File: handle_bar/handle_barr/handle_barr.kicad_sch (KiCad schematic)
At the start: 18 parts, among them J1 SPKR, J2 MAX98357A 3V3, J3 HRN_SW, J4 BAT, J5 PS2, J6 USB, U1 XIAO_ESP32C3, U2 MCP73831-2-OT

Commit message: add joystick support on case
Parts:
- added GPS1: NEO6M, solderwirepad_1_02_SMD:SolderWirePad_1x04_SMD_1x3mm, symbol Connector_Generic:Conn_01x04
- renumbered R2 to R1, R1 to R2
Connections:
- net +3.3V: now also GPS1.1 (Pin_1)
- net GND: now also GPS1.4 (Pin_4)
- net SW_JS: now also U1.3 (D2); no longer U1.8 (RX_D7)
- net RX: now reaches U1.7 (TX_D6)
- net RX: now also GPS1.2 (Pin_2)
- new net TX: GPS1.3 (Pin_3), U1.8 (RX_D7)
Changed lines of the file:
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@@
     (stroke (width 0) (type default) (color 0 0 0 0))
   )
+  (global_label "RX" (shape input) (at 52.07 87.63 180) (fields_autoplaced)
+    (effects (font (size 1 1)) (justify right))
+    (property "Intersheet References" "${INTERSHEET_REFS}" (id 0) (at 48.2176 87.5675 0)
+      (effects (font (size 1 1)) (justify right) hide)
+    )
+  )
   (global_label "VDD" (shape input) (at 255.27 29.21 180) (fields_autoplaced)
     (effects (font (size 1 1)) (justify right))
@@
     (effects (font (size 1 1)) (justify left))
     (property "Intersheet References" "${INTERSHEET_REFS}" (id 0) (at 212.751 105.4725 0)
-      (effects (font (size 1 1)) (justify left) hide)
-    )
-  )
-  (global_label "SW_JS" (shape input) (at 78.74 48.26 0) (fields_autoplaced)
-    (effects (font (size 1 1)) (justify left))
-    (property "Intersheet References" "${INTERSHEET_REFS}" (id 0) (at 85.2114 48.3225 0)
       (effects (font (size 1 1)) (justify left) hide)
     )
@@
     )
   )
+  (global_label "SW_JS" (shape input) (at 43.18 50.8 180) (fields_autoplaced)
+    (effects (font (size 1 1)) (justify right))
+    (property "Intersheet References" "${INTERSHEET_REFS}" (id 0) (at 36.7086 50.7375 0)
+      (effects (font (size 1 1)) (justify right) hide)
+    )
+  )
+  (global_label "3V3" (shape input) (at 52.07 85.09 180) (fields_autoplaced)
+    (effects (font (size 1 1)) (justify right))
+    (property "Intersheet References" "${INTERSHEET_REFS}" (id 0) (at 47.4081 85.0275 0)
+      (effects (font (size 1 1)) (justify right) hide)
+    )
+  )
   (global_label "LED_DIN" (shape input) (at 104.14 43.18 180) (fields_autoplaced)
     (effects (font (size 1 1)) (justify right))
@@
     )
   )
+  (global_label "TX" (shape input) (at 52.07 90.17 180) (fields_autoplaced)
+    (effects (font (size 1 1)) (justify right))
+    (property "Intersheet References" "${INTERSHEET_REFS}" (id 0) (at 48.4557 90.1075 0)
+      (effects (font (size 1 1)) (justify right) hide)
+    )
+  )
   (global_label "DIN" (shape input) (at 43.18 53.34 180) (fields_autoplaced)
     (effects (font (size 1 1)) (justify right))
@@
     )
   )
+  (global_label "RX" (shape input) (at 78.74 45.72 0) (fields_autoplaced)
+    (effects (font (size 1 1)) (justify left))
+    (property "Intersheet References" "${INTERSHEET_REFS}" (id 0) (at 82.5924 45.7825 0)
+      (effects (font (size 1 1)) (justify left) hide)
+    )
+  )
+  (global_label "TX" (shape input) (at 78.74 48.26 0) (fields_autoplaced)
+    (effects (font (size 1 1)) (justify left))
+    (property "Intersheet References" "${INTERSHEET_REFS}" (id 0) (at 82.3543 48.3225 0)
+      (effects (font (size 1 1)) (justify left) hide)
+    )
+  )
   (global_label "GND" (shape input) (at 161.29 50.8 270) (fields_autoplaced)
     (effects (font (size 1 1)) (justify right))
@@
     (effects (font (size 1 1)) (justify right))
     (property "Intersheet References" "${INTERSHEET_REFS}" (id 0) (at 201.269 93.9175 0)
+      (effects (font (size 1 1)) (justify right) hide)
+    )
+  )
+  (global_label "GND" (shape input) (at 52.07 92.71 180) (fields_autoplaced)
+    (effects (font (size 1 1)) (justify right))
+    (property "Intersheet References" "${INTERSHEET_REFS}" (id 0) (at 47.1224 92.6475 0)
       (effects (font (size 1 1)) (justify right) hide)
     )
@@
     (pin "2")
   )
+  (symbol (lib_id "Connector_Generic:Conn_01x04") (at 57.15 87.63 0) (unit 1)
+    (in_bom yes) (on_board yes) (fields_autoplaced)
+    (property "Reference" "GPS1" (id 0) (at 59.69 87.6299 0)
+      (effects (font (size 1.27 1.27)) (justify left))
+    )
+    (property "Value" "NEO6M" (id 1) (at 59.69 90.1699 0)
+      (effects (font (size 1.27 1.27)) (justify left))
+    )
+    (property "Footprint" "solderwirepad_1_02_SMD:SolderWirePad_1x04_SMD_1x3mm" (id 2) (at 57.15 87.63 0)
+      (effects (font (size 1.27 1.27)) hide)
+    )
+    (property "Datasheet" "~" (id 3) (at 57.15 87.63 0)
+      (effects (font (size 1.27 1.27)) hide)
+    )
+    (pin "1")
+    (pin "2")
+    (pin "3")
+    (pin "4")
+  )
   (symbol (lib_id "power:GND") (at 238.76 82.55 0) (unit 1)
     (in_bom yes) (on_board yes) (fields_autoplaced)
@@
   (symbol (lib_id "Device:R") (at 149.86 99.06 0) (unit 1)
     (in_bom yes) (on_board yes)
-    (property "Reference" "R1" (id 0) (at 152.4 97.7899 0)
+    (property "Reference" "R2" (id 0) (at 152.4 97.7899 0)
       (effects (font (size 1.27 1.27)) (justify left))
     )
@@
   (symbol (lib_id "Device:R") (at 124.46 60.96 0) (unit 1)
     (in_bom yes) (on_board yes)
-    (property "Reference" "R2" (id 0) (at 127 59.6899 0)
+    (property "Reference" "R1" (id 0) (at 127 59.6899 0)
       (effects (font (size 1.27 1.27)) (justify left))
     )
@@
       (reference "D3") (unit 1) (value "WS2812B") (footprint "LED_SMD:LED_WS2812B_PLCC4_5.0x5.0mm_P3.2mm")
     )
+    (path "/14bdadf0-0709-4db7-9ed8-923b0e90bab6"
+      (reference "GPS1") (unit 1) (value "NEO6M") (footprint "solderwirepad_1_02_SMD:SolderWirePad_1x04_SMD_1x3mm")
+    )
     (path "/e1e1705c-e817-43c7-a6f2-583284baedae"
       (reference "J1") (unit 1) (value "SPKR") (footprint "")
@@
       (reference "PWR1") (unit 1) (value "SW_SPST") (footprint "solderwirepad_1_02_SMD:SolderWirePad_1x02_SMD_5x5mm")
     )
+    (path "/6d0b0be1-d31b-48c6-a8f6-1f65e558fbc9"
+      (reference "R1") (unit 1) (value "220ko") (footprint "Resistor_THT:R_Axial_DIN0207_L6.3mm_D2.5mm_P7.62mm_Horizontal")
+    )
     (path "/38f240f4-b45a-498e-b92b-89acdf6f6e3d"
-      (reference "R1") (unit 1) (value "2kΩ") (footprint "Resistor_THT:R_Axial_DIN0207_L6.3mm_D2.5mm_P7.62mm_Horizontal")
-    )
-    (path "/6d0b0be1-d31b-48c6-a8f6-1f65e558fbc9"
-      (reference "R2") (unit 1) (value "220ko") (footprint "Resistor_THT:R_Axial_DIN0207_L6.3mm_D2.5mm_P7.62mm_Horizontal")
+      (reference "R2") (unit 1) (value "2kΩ") (footprint "Resistor_THT:R_Axial_DIN0207_L6.3mm_D2.5mm_P7.62mm_Horizontal")
     )
     (path "/9e8719a0-1e3e-4a7f-a6ab-4c947d699615"

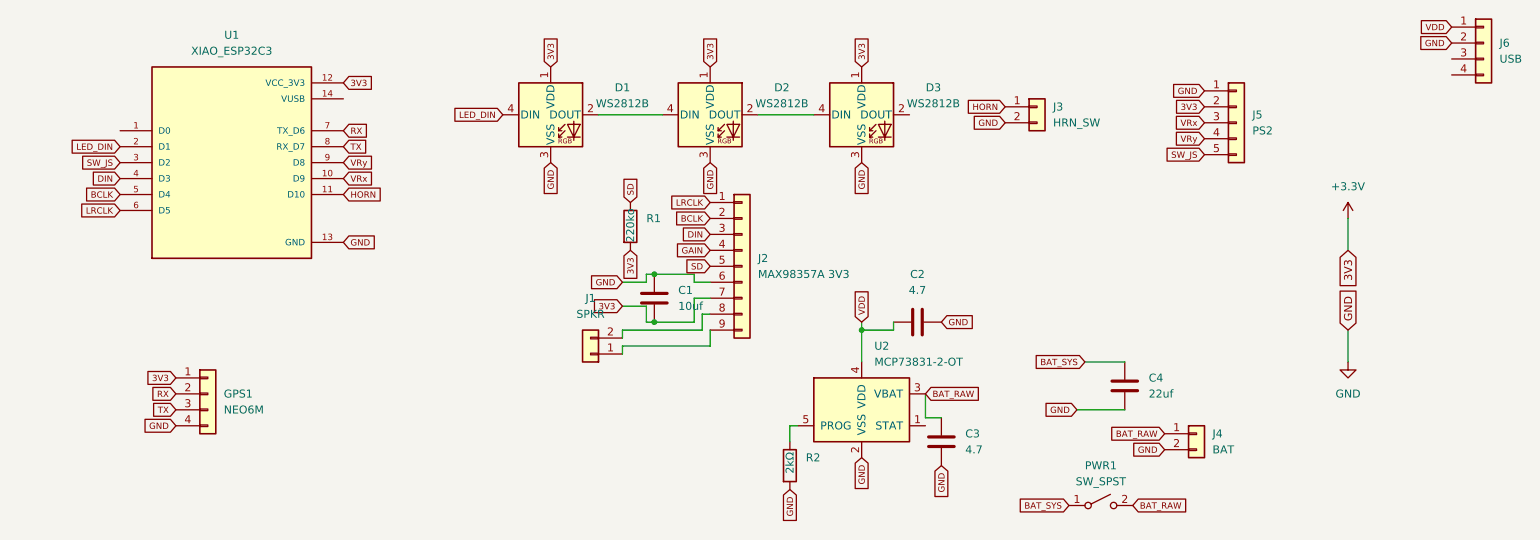
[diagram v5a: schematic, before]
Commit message: ad poped display for indicator lights, made seprate pcb for daisy lights.
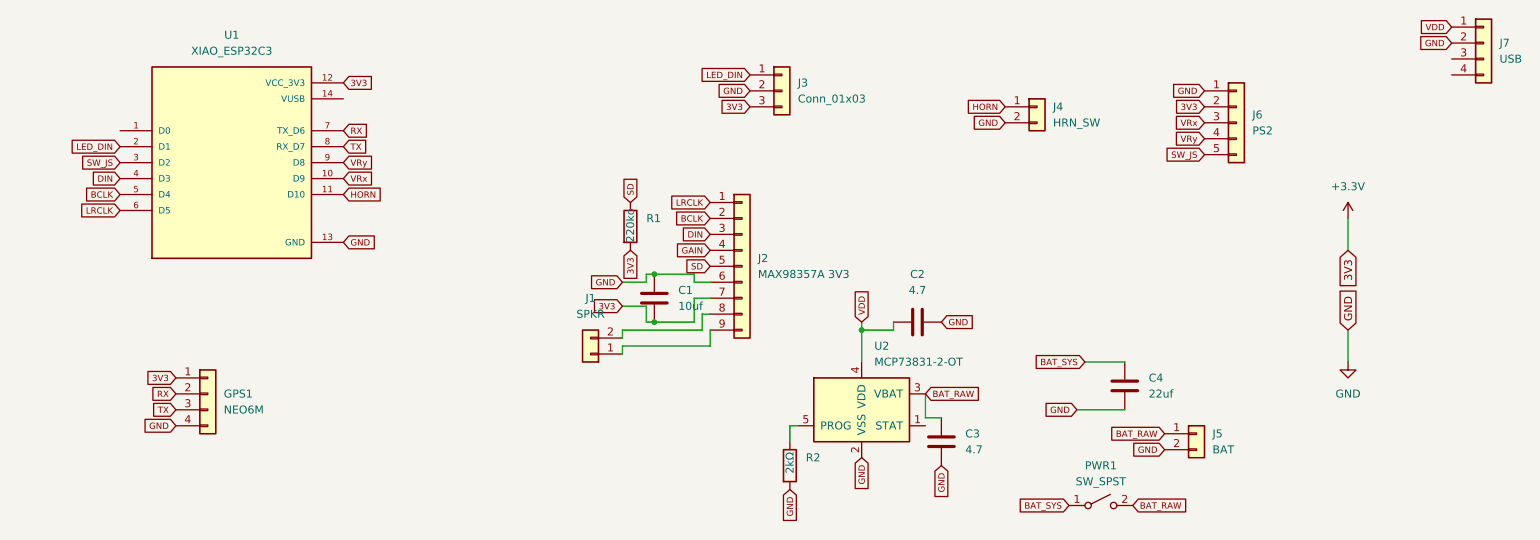
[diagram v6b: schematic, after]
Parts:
- removed D1, D2, D3: WS2812B, LED_SMD:LED_WS2812B_PLCC4_5.0x5.0mm_P3.2mm, symbol LED:WS2812B
- added J3: Conn_01x03, solderwirepad_1_02_SMD:SolderWirePad_1x03_SMD_1x3mm, symbol Connector_Generic:Conn_01x03
- renumbered J3 to J4, J4 to J5, J5 to J6, J6 to J7
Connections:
- net +3.3V: now also J3.3 (Pin_3)
- net GND: now also J3.2 (Pin_2)
- net LED_DIN: now also J3.1 (Pin_1)
